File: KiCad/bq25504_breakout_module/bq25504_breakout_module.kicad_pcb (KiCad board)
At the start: 2 copper layers, 29 x 45 mm, 22 parts, among them J1 Vin, J2 Output, U1 BQ25504

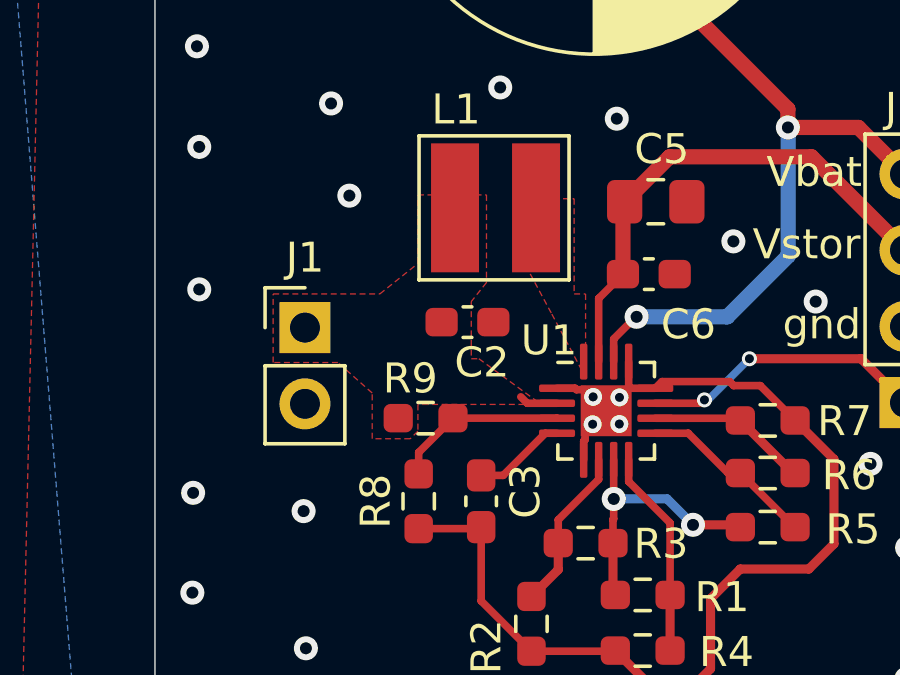
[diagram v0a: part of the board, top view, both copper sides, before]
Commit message: updated bq25504
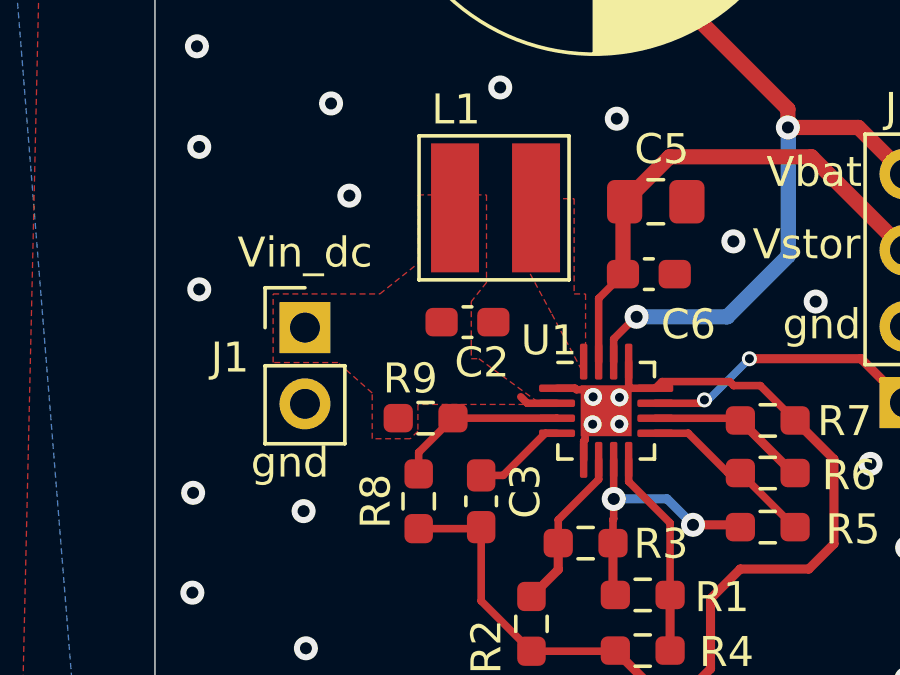
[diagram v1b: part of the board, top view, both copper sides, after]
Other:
- board text added: "Vin_dc"
